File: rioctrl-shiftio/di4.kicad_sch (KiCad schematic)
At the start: 3 parts, among them U10 ELQ3H4

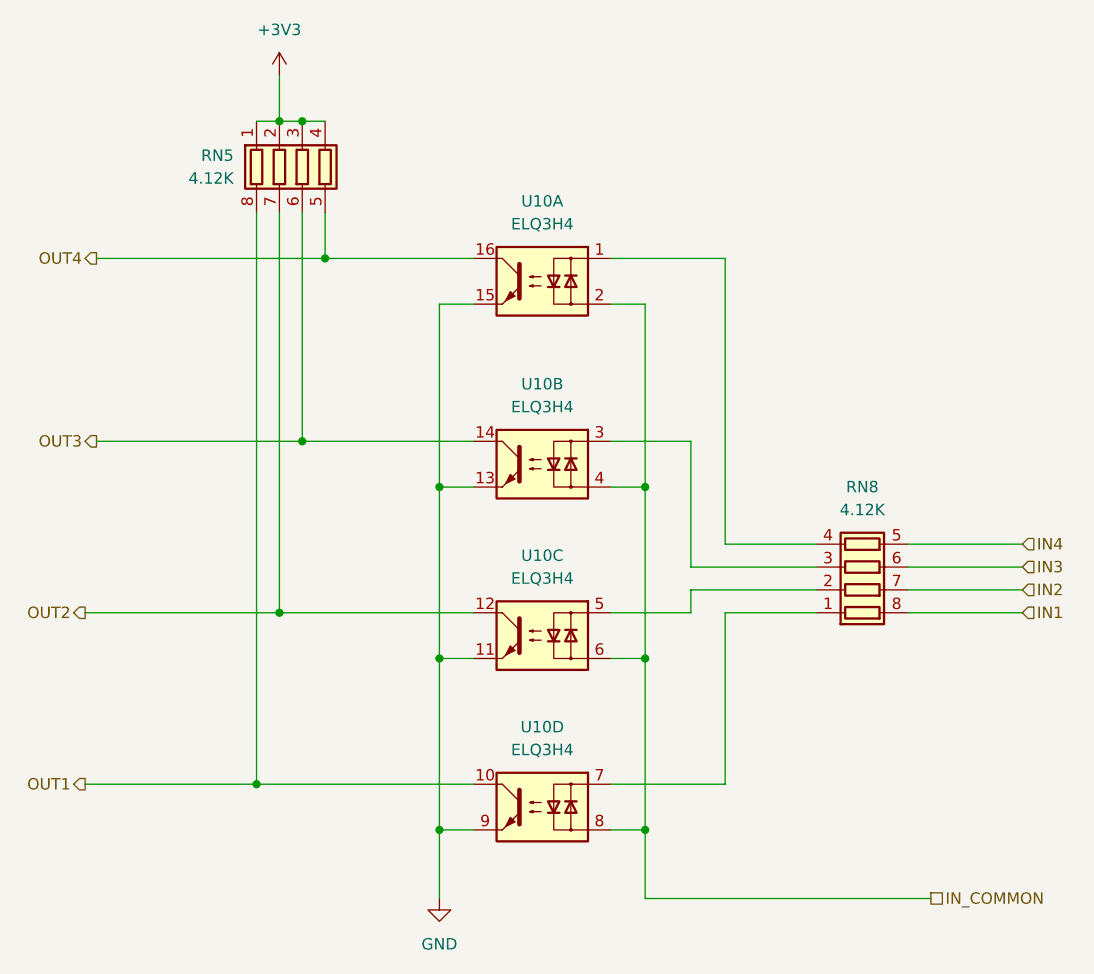
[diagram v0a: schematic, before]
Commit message: Fill in BOM (LCSC#)
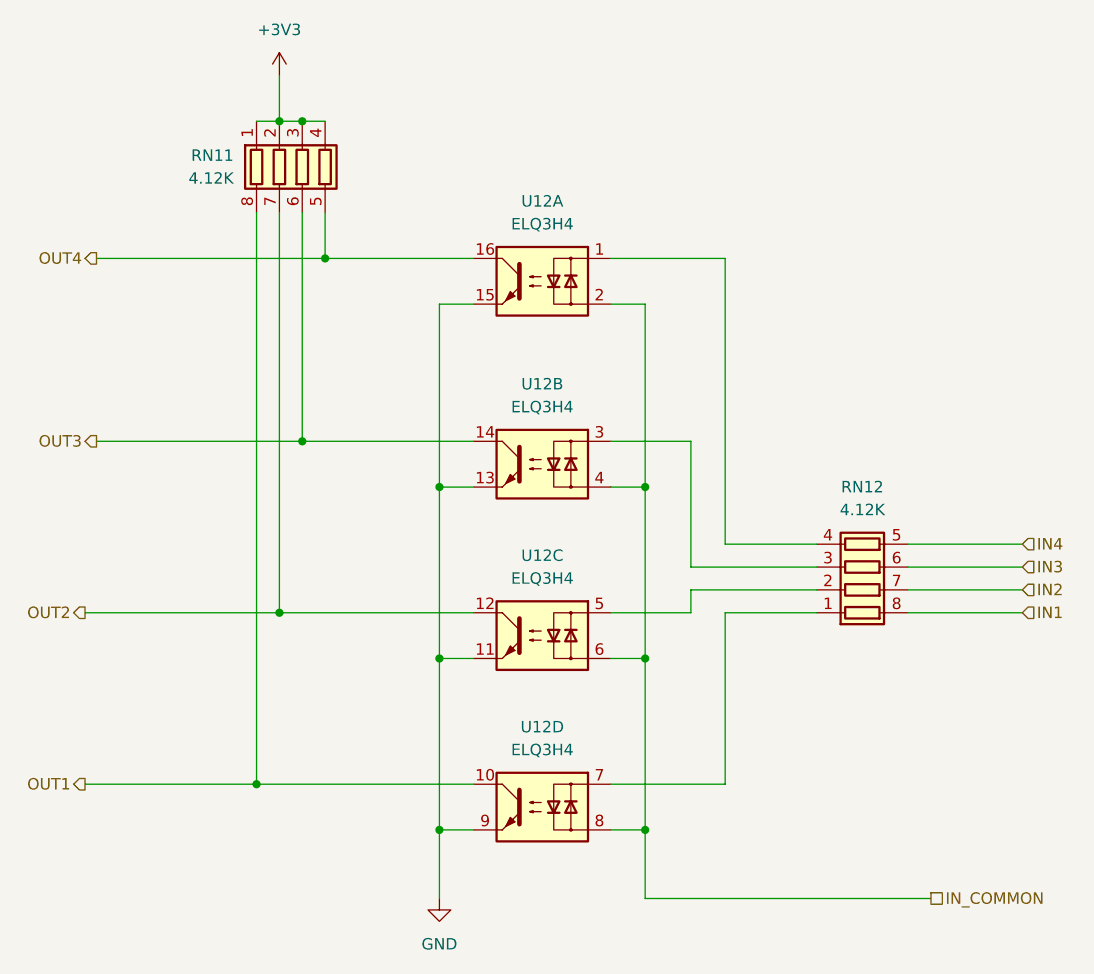
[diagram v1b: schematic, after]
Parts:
- RN11: renamed from RN5; LCSC# (none) -> C728970
- RN12: renamed from RN8; LCSC# (none) -> C728970
- renumbered U10 to U12
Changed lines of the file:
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@@
 		(on_board yes)
 		(dnp no)
-		(property "Reference" "RN8"
+		(property "Reference" "RN12"
 			(at 167.64 86.36 90)
 			(effects
@@
 		)
 		(property "Description" "4 resistor network, parallel topology"
+			(at 167.64 95.25 0)
+			(effects
+				(font
+					(size 1.27 1.27)
+				)
+				(hide yes)
+			)
+		)
+		(property "LCSC#" "C728970"
 			(at 167.64 95.25 0)
 			(effects
@@
 		(on_board yes)
 		(dnp no)
-		(property "Reference" "RN5"
+		(property "Reference" "RN11"
 			(at 97.79 49.5299 0)
 			(effects
@@
 		)
 		(property "Description" "4 resistor network, parallel topology"
+			(at 105.41 50.8 0)
+			(effects
+				(font
+					(size 1.27 1.27)
+				)
+				(hide yes)
+			)
+		)
+		(property "LCSC#" "C728970"
 			(at 105.41 50.8 0)
 			(effects
@@
 		(dnp no)
 		(fields_autoplaced yes)
-		(property "Reference" "U10"
+		(property "Reference" "U12"
 			(at 132.08 93.98 0)
 			(effects
@@
 		(dnp no)
 		(fields_autoplaced yes)
-		(property "Reference" "#PWR032"
+		(property "Reference" "#PWR036"
 			(at 102.87 44.45 0)
 			(effects
@@
 		(dnp no)
 		(fields_autoplaced yes)
-		(property "Reference" "U10"
+		(property "Reference" "U12"
 			(at 132.08 113.03 0)
 			(effects
@@
 		(dnp no)
 		(fields_autoplaced yes)
-		(property "Reference" "U10"
+		(property "Reference" "U12"
 			(at 132.08 54.61 0)
 			(effects
@@
 		(dnp no)
 		(fields_autoplaced yes)
-		(property "Reference" "#PWR033"
+		(property "Reference" "#PWR037"
 			(at 120.65 138.43 0)
 			(effects
@@
 		(dnp no)
 		(fields_autoplaced yes)
-		(property "Reference" "U10"
+		(property "Reference" "U12"
 			(at 132.08 74.93 0)
 			(effects
